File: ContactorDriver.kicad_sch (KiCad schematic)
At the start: 35 parts, among them J1 PowerConn, J2 DashboardConnA, J3 ContactorAConn, J4 FanConn1, J5 FanConn2, J6 DashboardConnB, J7 ContactorBConn, J8 FanConn3, Q1 CSD18511KTT, Q2 CSD18511KTT, Q3 CSD18511KTT, U1 RI3-1212S

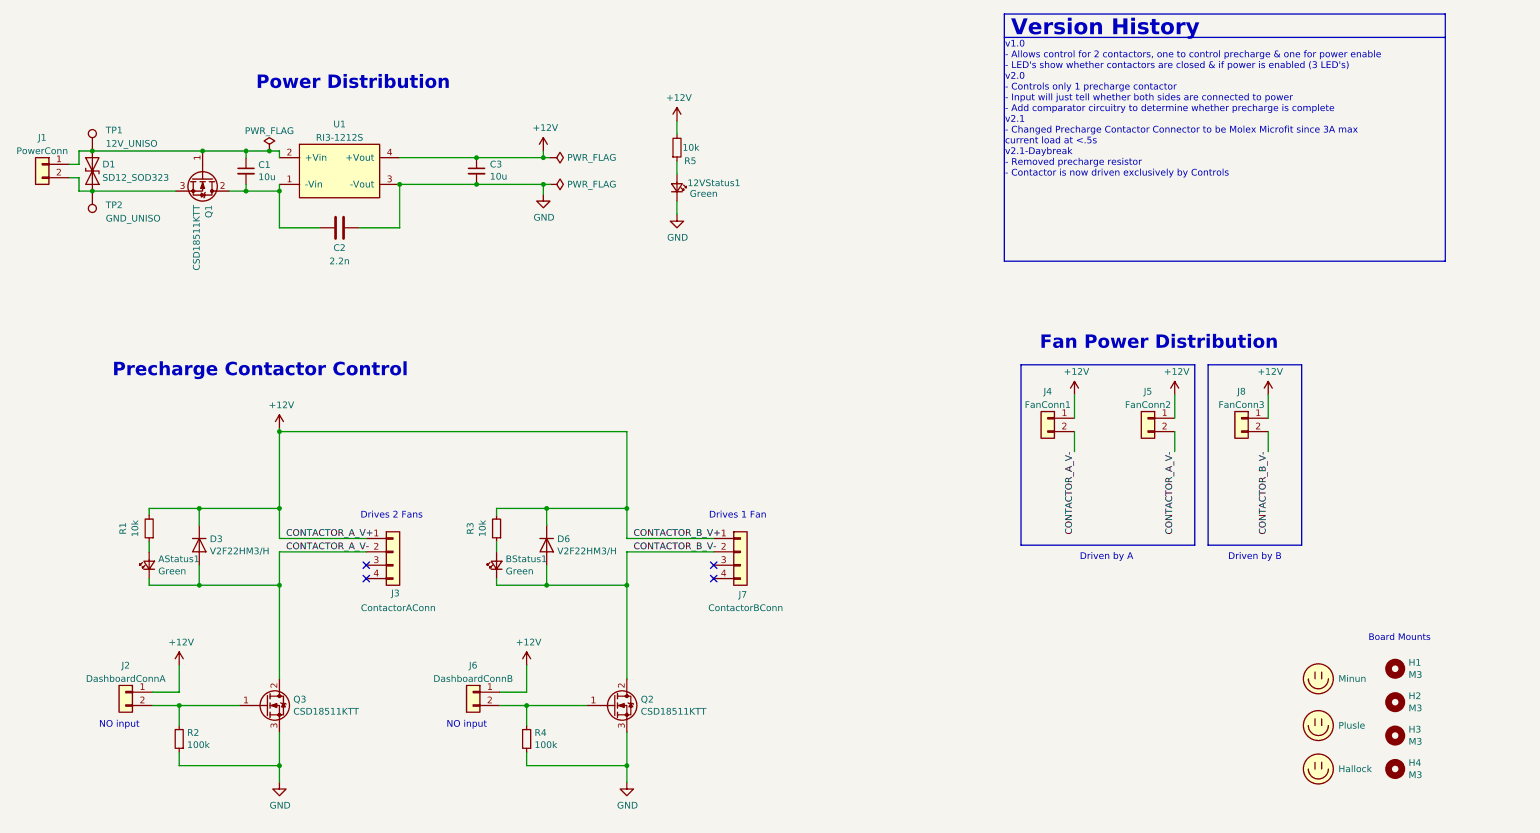
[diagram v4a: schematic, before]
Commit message: Updated with vertical conns, new mosfet, and no more isolator
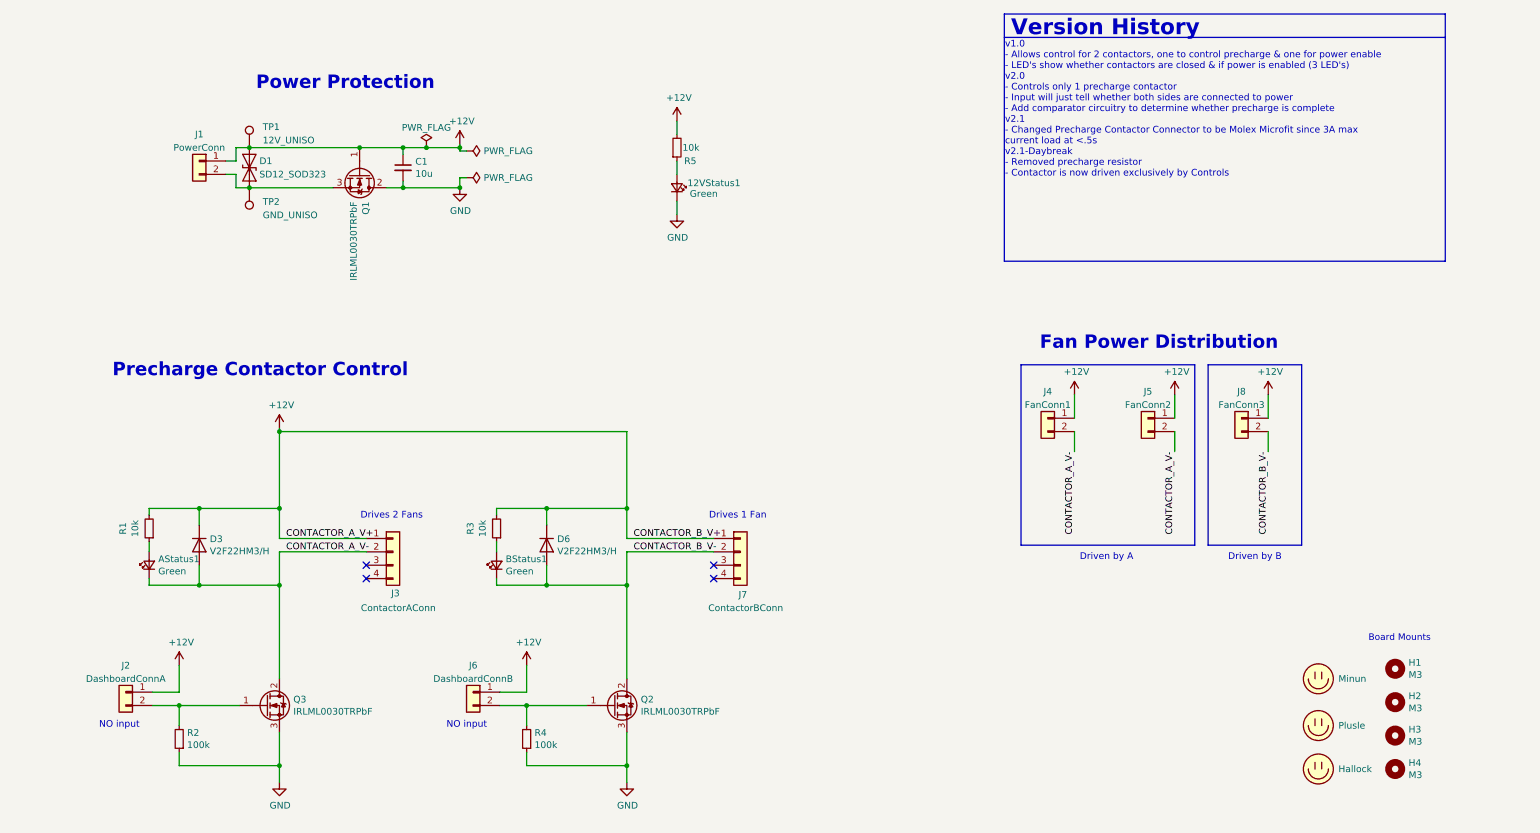
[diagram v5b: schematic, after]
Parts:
- removed C2: 2.2n, Capacitor_SMD:C_0805_2012Metric, symbol Device:C
- removed C3: 10u, Capacitor_SMD:C_0805_2012Metric, symbol Device:C_Small
- removed U1: RI3-1212S, UTSVT_ICs:RI3_DC_Converter, symbol utsvt-power-regulators:RI3-xxxxS
- J1, J2, J4, J5, J6, J8: footprint Connector_Molex:Molex_Micro-Fit_3.0_43650-0200_1x02_P3.00mm_Horizontal -> Connector_Molex:Molex_Micro-Fit_3.0_43650-0215_1x02_P3.00mm_Vertical
- Q1, Q2, Q3: value CSD18511KTT -> IRLML0030TRPbF; footprint Package_TO_SOT_SMD:TO-252-2 -> Package_TO_SOT_SMD:SOT-23
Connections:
- net +12V: now also C1.1, D1.2 (A2), J1.1 (Pin_1), Q1.1 (G), TP1.1
- net GND: now also C1.2, Q1.2 (D)
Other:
- note added: "Power Protection"
- note removed: "Power Distribution"
- moved on the sheet: C1, D1, J1, TP1, TP2

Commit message: Updated to all be 2 pin connectors
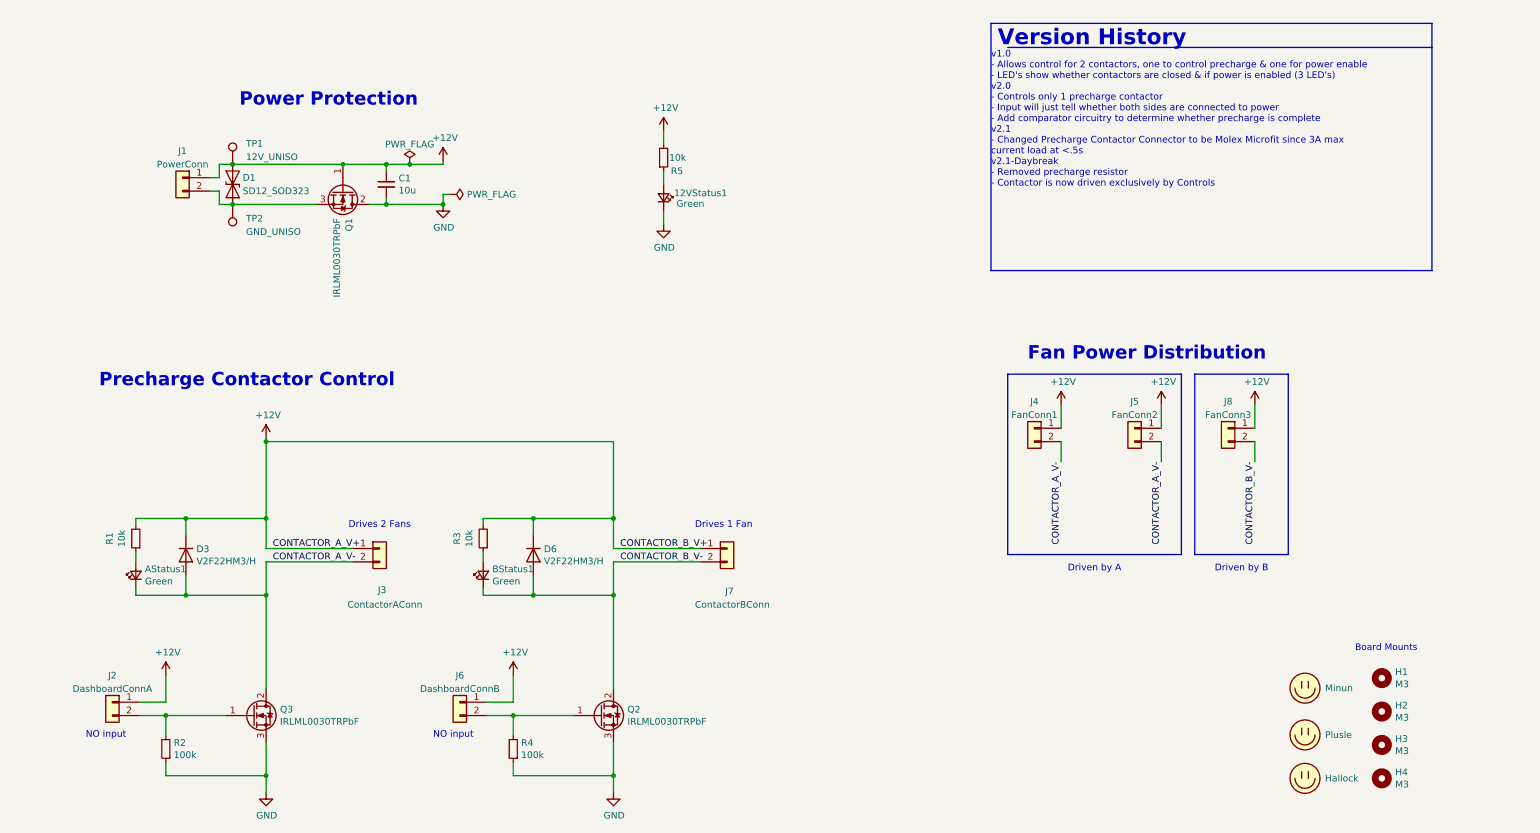
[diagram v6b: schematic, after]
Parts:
- J3, J7: footprint UTSVT_Connectors:Molex_MicroFit3.0_1x4xP3.00mm_PolarizingPeg_Vertical -> Connector_Molex:Molex_Micro-Fit_3.0_43650-0215_1x02_P3.00mm_Vertical; symbol Connector_Generic:Conn_01x04 -> Connector_Generic:Conn_01x02
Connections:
- no-connect marks 4 -> 0
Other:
- moved on the sheet: 12VStatus1, AStatus1, BStatus1, C1, D1, D3, D6, H1, H2, H3, H4, J1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

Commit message: Fixed warnings
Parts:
- renumbered 12VStatus1 to 12V1
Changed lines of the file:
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@@
 		(on_board yes)
 		(dnp no)
-		(property "Reference" "12VStatus1"
-			(at 148.59 46.101 90)
+		(property "Reference" "12V1"
+			(at 143.51 46.355 90)
 			(effects
 				(font
@@
 			(project "ContactorDriver"
 				(path "/aaa5c8ef-bb12-4c4a-bd2b-ddbca3d09ae8"
-					(reference "12VStatus1")
+					(reference "12V1")
 					(unit 1)
 				)

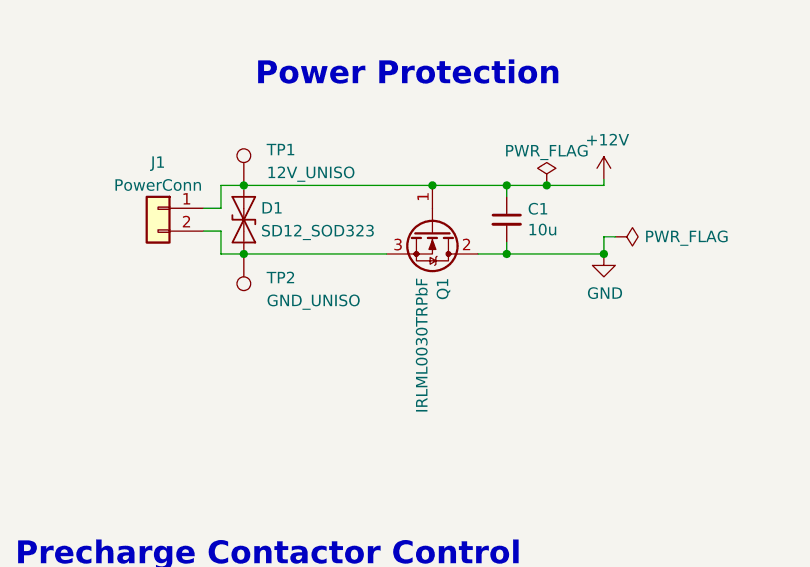
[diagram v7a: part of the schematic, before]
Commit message: Added labels for connectors
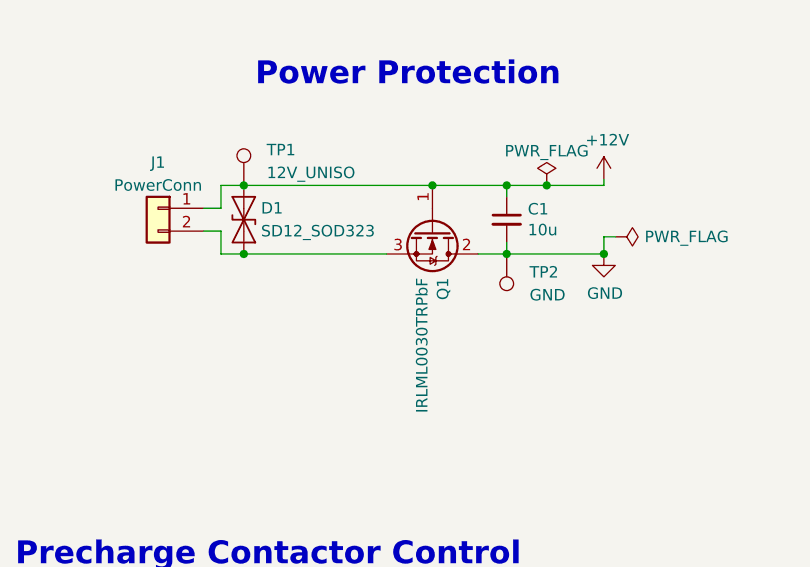
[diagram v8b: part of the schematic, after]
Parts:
- TP2: value GND_UNISO -> GND
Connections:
- net GND: now also TP2.1
- net at D1.1 (A1), J1.2 (Pin_2), Q1.3 (S): no longer TP2.1
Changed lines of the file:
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@@
+	(symbol
+		(lib_id "Connector:TestPoint")
+		(at 83.82 48.26 180)
+		(unit 1)
+		(exclude_from_sim no)
+		(in_bom yes)
+		(on_board yes)
+		(dnp no)
+		(fields_autoplaced yes)
+		(property "Reference" "TP2"
+			(at 86.36 50.2919 0)
+			(effects
+				(font
+					(size 1.27 1.27)
+				)
+				(justify right)
+			)
+		)
+		(property "Value" "GND"
+			(at 86.36 52.8319 0)
+			(effects
+				(font
+					(size 1.27 1.27)
+				)
+				(justify right)
+			)
+		)
+		(property "Footprint" "TestPoint:TestPoint_Keystone_5005-5009_Compact"
+			(at 78.74 48.26 0)
+			(effects
+				(font
+					(size 1.27 1.27)
+				)
+				(hide yes)
+			)
+		)
+		(property "Datasheet" "~"
+			(at 78.74 48.26 0)
+			(effects
+				(font
+					(size 1.27 1.27)
+				)
+				(hide yes)
+			)
+		)
+		(property "Description" ""
+			(at 83.82 48.26 0)
+			(effects
+				(font
+					(size 1.27 1.27)
+				)
+				(hide yes)
+			)
+		)
+		(pin "1"
+		)
+		(instances
+			(project "ContactorDriver"
+				(path "/aaa5c8ef-bb12-4c4a-bd2b-ddbca3d09ae8"
+					(reference "TP2")
+					(unit 1)
+				)
+			)
+		)
+	)
 	(symbol
 		(lib_id "Connector:TestPoint")
@@
 					(unit 1)
 				)
-			)
-		)
-	)
-	(symbol
-		(lib_id "Connector:TestPoint")
-		(at 54.61 48.26 180)
-		(unit 1)
-		(exclude_from_sim no)
-		(in_bom yes)
-		(on_board yes)
-		(dnp no)
-		(fields_autoplaced yes)
-		(property "Reference" "TP2"
-			(at 57.15 50.927 0)
-			(effects
-				(font
-					(size 1.27 1.27)
-				)
-				(justify right)
-			)
-		)
-		(property "Value" "GND_UNISO"
-			(at 57.15 53.467 0)
-			(effects
-				(font
-					(size 1.27 1.27)
-				)
-				(justify right)
-			)
-		)
-		(property "Footprint" "TestPoint:TestPoint_Keystone_5005-5009_Compact"
-			(at 49.53 48.26 0)
-			(effects
-				(font
-					(size 1.27 1.27)
-				)
-				(hide yes)
-			)
-		)
-		(property "Datasheet" "~"
-			(at 49.53 48.26 0)
-			(effects
-				(font
-					(size 1.27 1.27)
-				)
-				(hide yes)
-			)
-		)
-		(property "Description" ""
-			(at 54.61 48.26 0)
-			(effects
-				(font
-					(size 1.27 1.27)
-				)
-				(hide yes)
-			)
-		)
-		(pin "1"
-		)
-		(instances
-			(project "ContactorDriver"
-				(path "/aaa5c8ef-bb12-4c4a-bd2b-ddbca3d09ae8"
-					(reference "TP2")
-					(unit 1)
-				)
